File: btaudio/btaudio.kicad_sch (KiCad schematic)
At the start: 52 parts, among them J1 BAT_CON, J2 USB_C_Receptacle_USB2.0_16P, J4 AudioJack4, SW1 POWER_SW, SW2 PLAY/VOL+, SW3 PAUSE/VOL-, SW4 PREV/BT PAIRING, SW5 NEXT/BT DISCONNECT, SW6 SOFT RESET, U1 EWM104-BT5125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

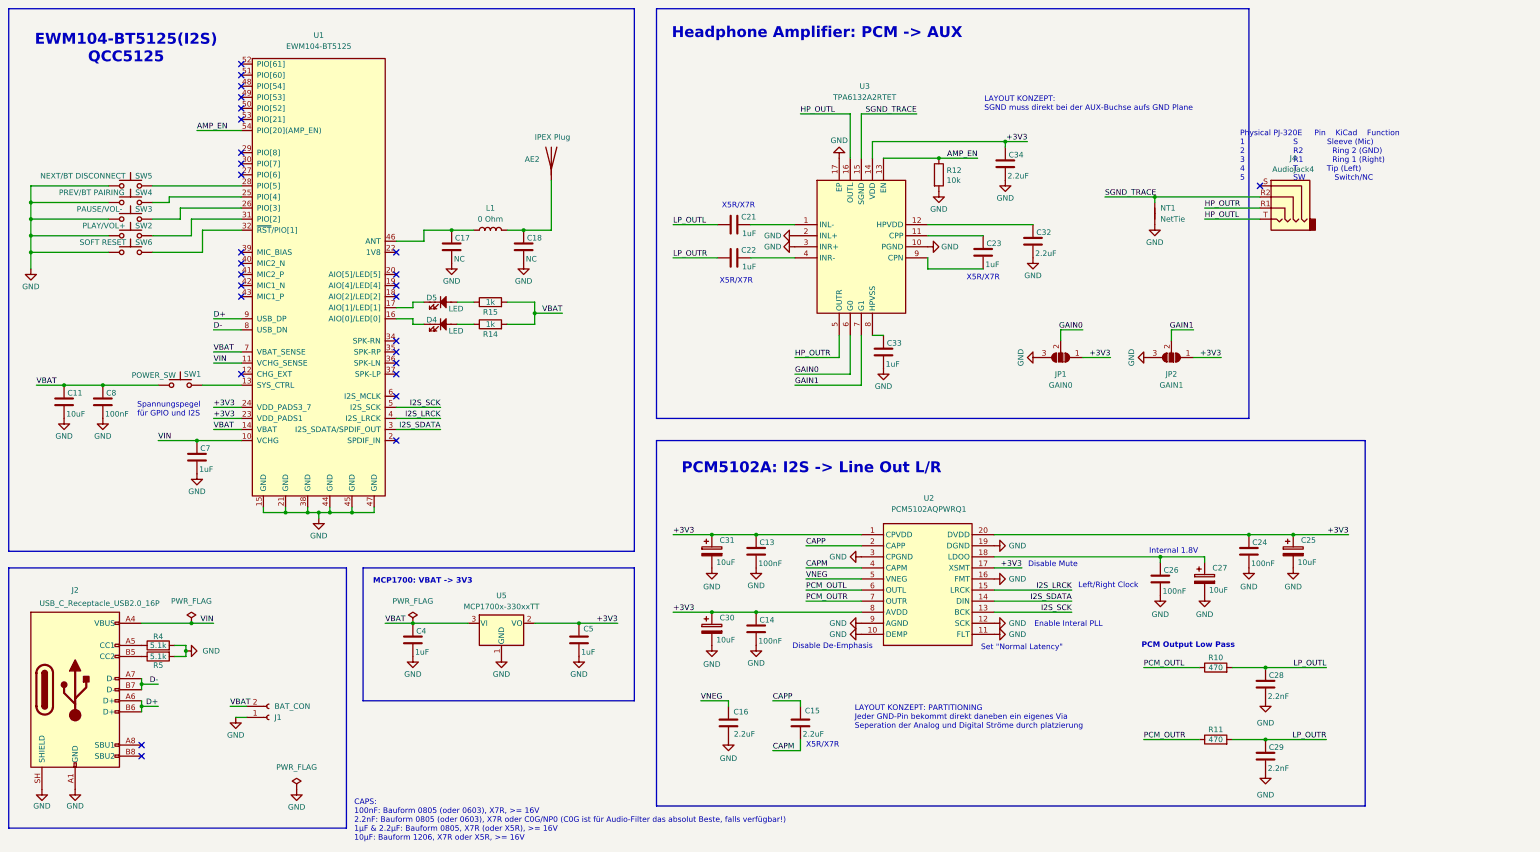
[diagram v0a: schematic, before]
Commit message: compacting layout
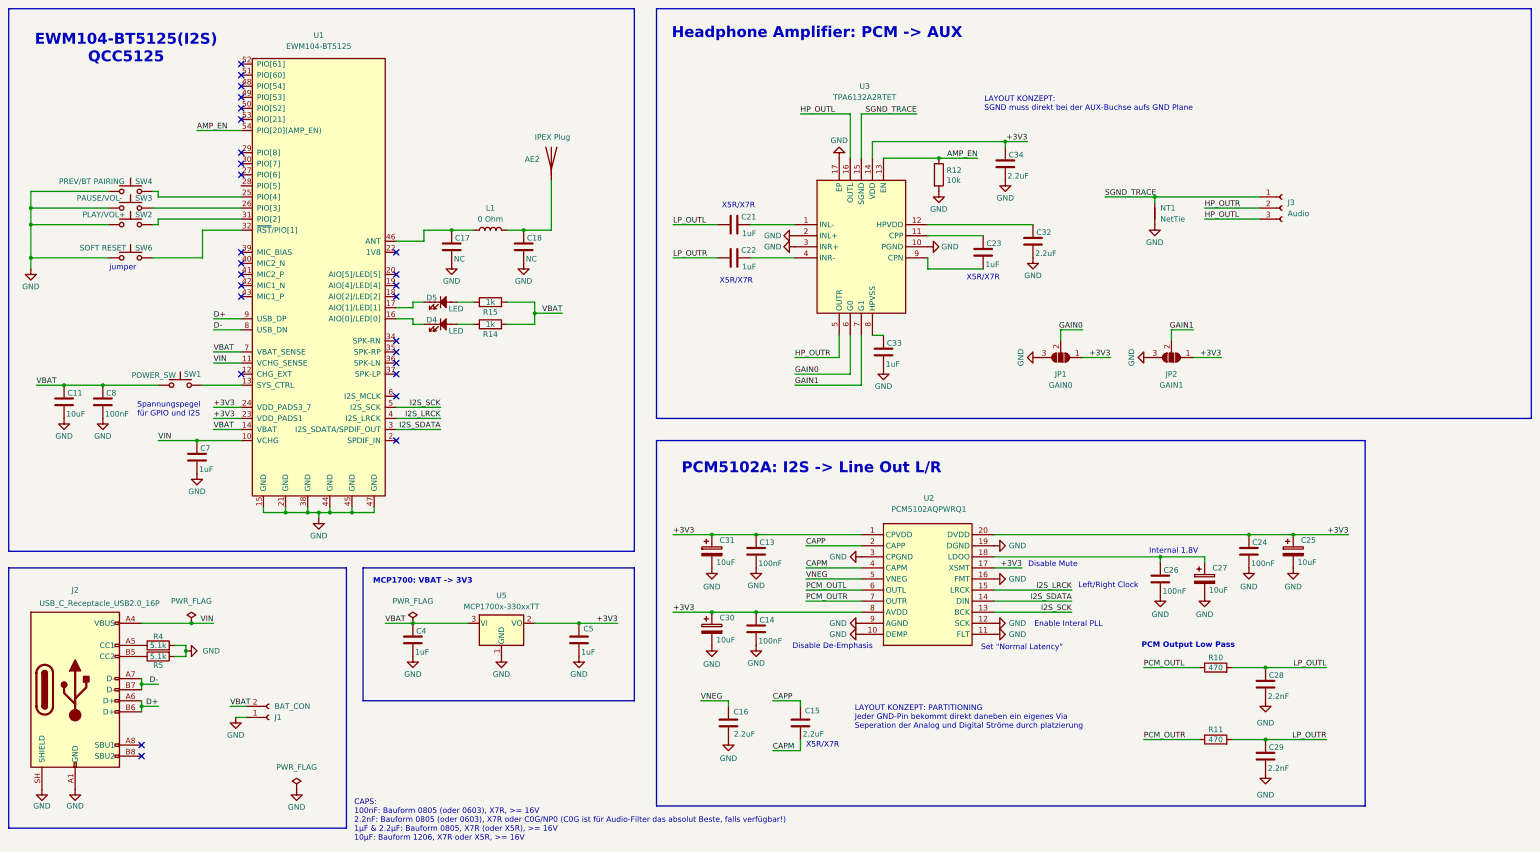
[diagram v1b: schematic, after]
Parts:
- removed J4: AudioJack4, Connector_Audio:Jack_3.5mm_PJ320E_Horizontal, symbol Connector_Audio:AudioJack4
- removed SW5: NEXT/BT DISCONNECT, Button_Switch_SMD:SW_SPST_TS-1088-xR020, symbol Switch:SW_Push
- added J3: Audio, PCM_Crystal_Handsoldering_AKL:Resonator_SMD-3Pin_7.2x3.0mm_BigPads, symbol Connector:Conn_01x03_Socket
- C11, C25, C27, C30, C31: footprint Capacitor_SMD:C_1206_3216Metric_Pad1.33x1.80mm_HandSolder -> Capacitor_SMD:C_1206_3216Metric
- C13, C14, C15, C16, C21, C22, C23, C24, C26, C28, C29, C32, C33, C34, C4, C5, C7, C8: footprint Capacitor_SMD:C_0805_2012Metric_Pad1.18x1.45mm_HandSolder -> Capacitor_SMD:C_0805_2012Metric
- D4, D5: footprint LED_SMD:LED_0805_2012Metric_Pad1.15x1.40mm_HandSolder -> LED_SMD:LED_0805_2012Metric
- R10, R11, R12, R14, R15, R4, R5: footprint Resistor_SMD:R_0805_2012Metric_Pad1.20x1.40mm_HandSolder -> Resistor_SMD:R_0805_2012Metric
- SW6: footprint Button_Switch_SMD:SW_SPST_TS-1088-xR020 -> Jumper:SolderJumper-2_P1.3mm_Open_RoundedPad1.0x1.5mm
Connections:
- net HP_OUTL: now also J3.3 (Pin_3)
- net HP_OUTR: now also J3.2 (Pin_2)
- net SGND_TRACE: now also J3.1 (Pin_1)
- no-connect marks 28 -> 27
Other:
- note added: "jumper"
- note removed: "Physical PJ-320E Pin KiCad Function 1 S Sleeve (Mic) 2 R2 Ring 2 (GND) 3 R1 Ring 1 (Right) 4 T Tip (Left) 5 SW Switch/NC"
- moved on the sheet: SW2, SW3, SW4, SW6

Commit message: primary layout done
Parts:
- removed J1: BAT_CON, Connector_JST:JST_SH_SM02B-SRSS-TB_1x02-1MP_P1.00mm_Horizontal, symbol Connector:Conn_01x02_Socket
- removed SW2: PLAY/VOL+, Button_Switch_SMD:SW_SPST_TS-1088-xR020, symbol Switch:SW_Push
- removed SW3: PAUSE/VOL-, Button_Switch_SMD:SW_SPST_TS-1088-xR020, symbol Switch:SW_Push
- removed SW4: PREV/BT PAIRING, Button_Switch_SMD:SW_SPST_TS-1088-xR020, symbol Switch:SW_Push
- added J1: BTNS, Connector_PinHeader_2.54mm:PinHeader_1x04_P2.54mm_Vertical, symbol Connector:Conn_01x04_Socket
- added J6: Battery, Connector_PinHeader_2.54mm:PinHeader_1x02_P2.54mm_Vertical, symbol Connector:Conn_01x02_Socket
- J3: footprint PCM_Crystal_Handsoldering_AKL:Resonator_SMD-3Pin_7.2x3.0mm_BigPads -> Aux-Pads:aux-pads
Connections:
- net GND: now also J1.1 (Pin_1), J6.2 (Pin_2)
- net VBAT: now also J6.1 (Pin_1)
- net at U1.26 (PIO[3]): now also J1.3 (Pin_3)
- net at U1.31 (PIO[2]): now also J1.2 (Pin_2)
- net at U1.25 (PIO[4]): now also J1.4 (Pin_4)
- no-connect marks 27 -> 28
